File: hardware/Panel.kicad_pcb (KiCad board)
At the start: 2 copper layers, 65.3 x 64.1 mm, 33 parts, among them J101 Conn_01x02, J102 Header, J103 Header, J104 Conn_01x02, J201 Conn_01x02, J202 Conn_01x02, J203 SSD1306, SW101 Rotary Encoder + Switch, SW102 10mm, SW103 10mm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

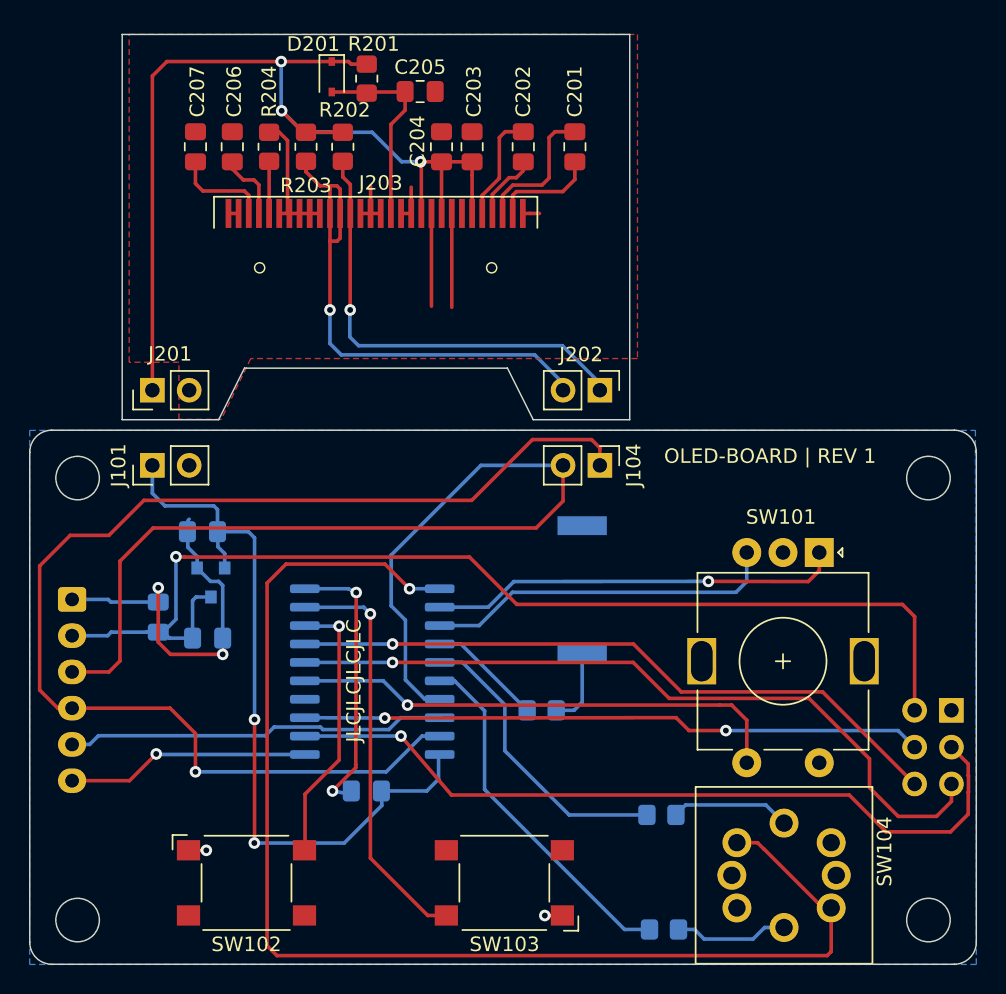
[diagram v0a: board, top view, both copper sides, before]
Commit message: Rev2 fixes
- Move I2C pullups on main board
- Fix left/right/main buttons traces
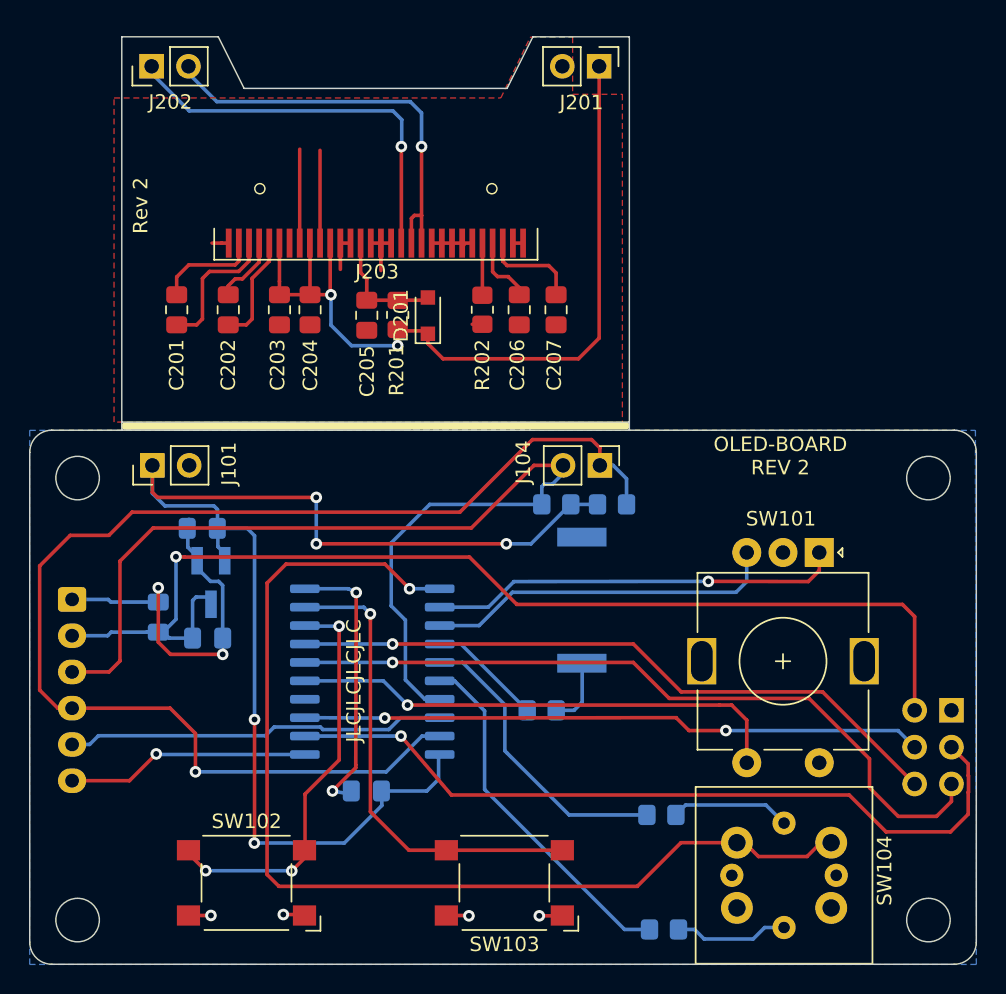
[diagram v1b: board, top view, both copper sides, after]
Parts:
- removed R203: 10K, Resistor_SMD:R_0805_2012Metric_Pad1.20x1.40mm_HandSolder
- removed R204: 910K, Resistor_SMD:R_0805_2012Metric_Pad1.20x1.40mm_HandSolder
- added R102: 10K, Resistor_SMD:R_0805_2012Metric_Pad1.20x1.40mm_HandSolder, B.Cu at (106.2, 88.5)
- added R103: 10K, Resistor_SMD:R_0805_2012Metric_Pad1.20x1.40mm_HandSolder, B.Cu at (110.0, 88.5)
- D201: footprint Diode_SMD:D_SOD-323 -> Diode_SMD:D_SOD-323_HandSoldering
- R202: value 10K -> 910K
- U101: footprint Package_TO_SOT_SMD:SOT-23 -> Package_TO_SOT_SMD:SOT-23_Handsoldering
- moved J202 38.1 mm to (78.3, 58.3), turned to 90 degrees
- moved J201 38.1 mm to (109.1, 58.3), turned to 270 degrees
- moved C201 29.7 mm to (80.0, 75.1), turned to 270 degrees
- moved C207 27.3 mm to (106.1, 75.1), turned to 270 degrees
- moved C202 23.2 mm to (83.5, 75.1), turned to 270 degrees
- moved C206 22.8 mm to (103.6, 75.1), turned to 270 degrees
- moved D201 17.8 mm to (97.3, 75.5), turned to 90 degrees
- moved C203 17.4 mm to (87.1, 75.1), turned to 270 degrees
- moved R201 16.4 mm to (95.2, 75.5), turned to 90 degrees
- moved C205 15.9 mm to (93.1, 75.5), turned to 270 degrees
- moved R202 14.8 mm to (101.1, 75.1)
- moved C204 14.4 mm to (89.2, 75.1), turned to 270 degrees
- moved J203 2.04 mm to (93.7, 70.5), turned to 0 degrees
- moved BZ101 0.79 mm to (107.9, 95.1)
- moved C103 0.23 mm to (81.7, 90.2)
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- renumbered R102 to R104, R103 to R105
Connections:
- R202 pad 1: SCL -> GND
- R202 pad 2: +3V3 -> Net-(J203-Pad26)
- SW102 pad 2: LBTN -> GND
- SW102 pad 3: (no net) -> LBTN
- SW102 pad 4: (no net) -> LBTN
- SW103 pad 2: RBTN -> GND
- SW103 pad 3: (no net) -> RBTN
- SW103 pad 4: (no net) -> RBTN
- SW104 pad 1: MBTN -> GND
- SW104 pad 4: GND -> MBTN
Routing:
- net +3V3: track 122.3 -> 146.1 mm, vias 5 -> 7
- net MBTN: track 89.8 -> 75.0 mm
- net LBTN: track 18.8 -> 28.7 mm, vias 1 -> 3
- net SDA: track 108.7 -> 101.1 mm
- net Net-(C205-Pad1): track 13.9 -> 8.42 mm
- net RBTN: track 28.4 -> 33.1 mm
- net Net-(R104-Pad2): track 9.13 -> 8.30 mm
- net Net-(BZ101-Pad1): track 5.50 -> 4.72 mm
- net GND: track 78.1 -> 77.5 mm, vias 6 -> 8
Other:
- board size 65.3 x 64.1 mm -> 65.3 x 64 mm
- board text added: "OLED-BOARD REV 2"
- board text added: "Rev 2"
- board text removed: "OLED-BOARD | REV 1"

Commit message: Moved oled pads
Moved oled pins by 2mm (they where too far from edge and were impossible to solder)
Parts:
- moved J203 2.00 mm to (93.7, 68.5)
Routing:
- net GND: track 77.5 -> 100.6 mm
- net +3V3: track 146.1 -> 152.0 mm
- net SDA: track 101.1 -> 97.2 mm
- net SCL: track 116.4 -> 114.0 mm
- net Net-(C205-Pad1): track 8.42 -> 10.4 mm
- net Net-(J203-Pad26): track 3.60 -> 5.60 mm
- net Net-(C201-Pad1): track 7.32 -> 9.32 mm
- net Net-(C207-Pad1): track 6.24 -> 8.24 mm
- net Net-(C206-Pad1): track 4.75 -> 6.75 mm
- net Net-(C202-Pad1): track 4.73 -> 6.73 mm
- net Net-(C201-Pad2): track 9.69 -> 11.7 mm
- net Net-(C202-Pad2): track 7.54 -> 9.54 mm
